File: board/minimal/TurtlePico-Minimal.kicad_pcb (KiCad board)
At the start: 2 copper layers, 121 parts, among them IC1 DRV8835DSSR, J1 Micro_SD, J10 LED, J11 LED, J12 Debug, J13 9DoF, J14 Temperature, J15 UltraSonic, J16 OLED, J2 USB_C_Receptacle_USB2.0_16P, J3 FR_ESC, J4 FL_ESC, J5 RMotor, J6 LMotor, J7 RR_ESC, J8 RL_ESC, J9 AudioJack3, Q1 DMP6050SSD, Q2 DMP6050SSD, Q3 2SC4213, Q4 2SC4213, SW1 SW_Bootsel, SW2 SW_RST, SW3 SW_{R}, SW4 SW_{L}, SW5 SW_DIP_x03, U1 W25Q128JVS, U10 PCM5102A, U2 AP63203WU, U3 RP2040, U4 STUSB4500QTR, U5 TLV73318PDBV, U6 PCA9306D, U7 ICM-20948, U8 BME280, U9 INA260, Y1 ABLS-12.000MHZ-B4-T

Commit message: set footprint
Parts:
- removed ? (x3): , 
- removed IC1: DRV8835DSSR, Package_SON:WSON-12-1EP_3x2mm_P0.5mm_EP1x2.65_ThermalVias
- removed Q4: 2SC4213, Package_TO_SOT_SMD:SOT-323_SC-70
- removed REF** (x4): MountingHole_3.2mm_M3_DIN965_Pad, MountingHole:MountingHole_3.2mm_M3_DIN965_Pad
- removed U10: PCM5102A, Package_SO:TSSOP-20_4.4x6.5mm_P0.65mm
- added C40: 0.01µ, Capacitor_SMD:C_0201_0603Metric, F.Cu at (123.6, 109.4)
- added C41: 10µ, Capacitor_SMD:CP_Elec_4x5.4, F.Cu at (109.4, 100.1)
- added C42: 10µ, Capacitor_SMD:CP_Elec_4x5.4, F.Cu at (109.4, 105.9)
- added C43: 10µ, Capacitor_SMD:CP_Elec_4x5.4, F.Cu at (109.4, 111.8)
- added J17: I/O Pins, Connector_PinSocket_2.54mm:PinSocket_2x08_P2.54mm_Vertical, F.Cu at (87.9, 41.2)
- added L2: 4.7u, AOTA-B201610S:L_pol_2016, F.Cu at (126.2, 66.8)
- added R30: 1k, Resistor_SMD:R_0603_1608Metric, F.Cu at (85.0, 74.6)
- added TP1: BNO_{BOOT}, TestPoint:TestPoint_Loop_D2.50mm_Drill1.85mm, F.Cu at (147.4, 94.0)
- added TP2: SPI_{MOSI}, TestPoint:TestPoint_Loop_D2.50mm_Drill1.85mm, F.Cu at (80.3, 41.6)
- added TP3: SPI_{SCK}, TestPoint:TestPoint_Loop_D2.50mm_Drill1.85mm, F.Cu at (80.3, 47.0)
- added TP4: SPI_{MISO}, TestPoint:TestPoint_Loop_D2.50mm_Drill1.85mm, F.Cu at (80.3, 52.5)
- added TP5: I2C_{SDA}, TestPoint:TestPoint_Loop_D2.50mm_Drill1.85mm, F.Cu at (80.3, 57.9)
- added TP6: I2C_{SCL}, TestPoint:TestPoint_Loop_D2.50mm_Drill1.85mm, F.Cu at (80.3, 63.4)
- added Y2: ABS06-32.768KHZ-T, ABRACON_Crystal:ABS06, F.Cu at (145.1, 107.7)
- C1, C2, C4, C6: value 100n -> 4.7u
- C12, C20, C3: value 1u -> 100n
- C14: value 10u -> 100n; footprint Capacitor_SMD:C_1206_3216Metric -> Capacitor_SMD:C_0201_0603Metric
- C15: value 22u -> 100n; footprint Capacitor_SMD:C_0402_1005Metric -> Capacitor_SMD:C_0201_0603Metric
- C16: value 22u -> 10u; footprint Capacitor_SMD:C_0402_1005Metric -> Capacitor_SMD:C_1206_3216Metric
- C17: value 27p -> 100n
- C18: value 27p -> 15p
- C19: value 1u -> 15p
- C21, C22: value 0.1u -> 22u; footprint Capacitor_SMD:C_0201_0603Metric -> Capacitor_SMD:C_0402_1005Metric
- C32, C33: value 0.01µ -> 100n
- C34, C35: value 10µ -> 20p; footprint Capacitor_SMD:CP_Elec_4x5.4 -> Capacitor_SMD:C_0201_0603Metric
- C36: value 10µ -> 2.2µ; footprint Capacitor_SMD:CP_Elec_4x5.4 -> Capacitor_SMD:C_0201_0603Metric
- C38: value 2.2µ -> 0.01µ
- J10: value LED -> AudioJack3; footprint Connector_PinSocket_2.54mm:PinSocket_1x02_P2.54mm_Vertical -> STX-3000:STX3000
- J12: value Debug -> LED; footprint Connector_JST:JST_PH_B3B-PH-SM4-TB_1x03-1MP_P2.00mm_Vertical -> Connector_PinSocket_2.54mm:PinSocket_1x02_P2.54mm_Vertical
- J13: value 9DoF -> UltraSonic; footprint Connector_JST:JST_XH_S4B-XH-A_1x04_P2.50mm_Horizontal -> Connector_PinSocket_2.54mm:PinSocket_1x04_P2.54mm_Vertical; moved to F.Cu
- J14: value Temperature -> Debug; footprint Connector_PinSocket_2.54mm:PinSocket_1x04_P2.54mm_Vertical -> Connector_JST:JST_PH_B3B-PH-SM4-TB_1x03-1MP_P2.00mm_Vertical
- J15: value UltraSonic -> Display; footprint Connector_PinSocket_2.54mm:PinSocket_1x04_P2.54mm_Vertical -> Connector_PinHeader_2.54mm:PinHeader_1x08_P2.54mm_Horizontal
- J16: value OLED -> TouchDisplay; footprint Connector_JST:JST_XH_S7B-XH-A_1x07_P2.50mm_Horizontal -> Connector_PinSocket_2.54mm:PinSocket_1x14_P2.54mm_Vertical; moved to F.Cu
- J2: value USB_C_Receptacle_USB2.0_16P -> Jack-DC; footprint Connector_USB:USB_C_Receptacle_GCT_USB4085 -> Connector_BarrelJack:BarrelJack_Horizontal; moved to F.Cu
- J3: value FR_ESC -> USB_C_Receptacle_USB2.0_16P; footprint Connector_PinHeader_2.54mm:PinHeader_1x03_P2.54mm_Horizontal -> Connector_USB:USB_C_Receptacle_GCT_USB4085; moved to F.Cu
- J4: value FL_ESC -> RMotor; footprint Connector_PinHeader_2.54mm:PinHeader_1x03_P2.54mm_Horizontal -> Connector_PinSocket_2.54mm:PinSocket_1x02_P2.54mm_Vertical; moved to F.Cu
- J5: value RMotor -> LMotor
- J6: value LMotor -> FR_ESC; footprint Connector_PinSocket_2.54mm:PinSocket_1x02_P2.54mm_Vertical -> Connector_PinHeader_2.54mm:PinHeader_1x03_P2.54mm_Horizontal
- J7: value RR_ESC -> FL_ESC; moved to F.Cu
- J8: value RL_ESC -> RR_ESC; moved to F.Cu
- J9: value AudioJack3 -> RL_ESC; footprint STX-3000:STX3000 -> Connector_PinHeader_2.54mm:PinHeader_1x03_P2.54mm_Horizontal; moved to F.Cu
- JP1: value I2C_Addr -> Jumper_Power; footprint Jumper:SolderJumper-2_P1.3mm_Open_RoundedPad1.0x1.5mm -> Connector_PinHeader_2.54mm:PinHeader_1x03_P2.54mm_Vertical
- JP2: value I2C_Addr -> Sens_SEL
- JP3: value Sens_SEL -> I2C_Addr
- L1: value 4.7u -> 3.3u; footprint Capacitor_SMD:C_0603_1608Metric -> AOTA-B201610S:L_pol_2016
- Q2: value DMP6050SSD -> 2SC4213; footprint Package_SO:SOIC-8_3.9x4.9mm_P1.27mm -> Package_TO_SOT_SMD:SOT-323_SC-70
- R1: value 27 -> 33
- R11: value 100k -> 1k
- R14, R21, R22: value 1k -> 10k
- R18: value 200k -> 100k
- R19: value 10k -> 1k
- R20: value 100k -> 10k
- R24, R25: value 5k -> 1k
- R26, R28: value 1k -> 5k
- R3, R7: value 1k -> 27
- R4, R5: value 10k -> 33
- R6: value 10k -> 27
- R8: value 1k -> 4.7k
- R9: value 10k -> 4.7k
- RV1: value 10k -> 50k; footprint Potentiometer_SMD:Potentiometer_ACP_CA6-VSMD_Vertical -> Potentiometer_THT:Potentiometer_Bourns_3339P_Vertical_HandSoldering
- SW2: value SW_RST -> SW_Reset
- SW5: value SW_DIP_x03 -> SW_DIP_x04; footprint DS04254203BKSMT:DS04254203BKSMT -> Package_DIP:DIP-8_W7.62mm
- U1: value W25Q128JVS -> RP2350B-QFN80; footprint Package_SO:SOIC-8_5.23x5.23mm_P1.27mm -> Package_DFN_QFN:QFN-80-1EP_10x10mm_P0.4mm_EP3.4x3.4mm_ThermalVias
- U2: value AP63203WU -> W25Q128JVS; footprint Package_TO_SOT_SMD:TSOT-23-6 -> Package_SO:SOIC-8_5.3x5.3mm_P1.27mm
- U3: value RP2040 -> AP63203WU; footprint Package_DFN_QFN:QFN-56-1EP_7x7mm_P0.4mm_EP3.2x3.2mm -> Package_TO_SOT_SMD:TSOT-23-6
- U5: value TLV73318PDBV -> DRV8835DSSR; footprint Package_TO_SOT_SMD:SOT-23-5 -> Package_SON:WSON-12-1EP_3x2mm_P0.5mm_EP1x2.65_ThermalVias
- U6: value PCA9306D -> INA260; footprint Package_SON:X2SON-8_1.4x1mm_P0.35mm -> Package_SO:TSSOP-16_4.4x5mm_P0.65mm
- U7: value ICM-20948 -> BNO086; footprint Sensor_Motion:InvenSense_QFN-24_3x3mm_P0.4mm -> BNO086:BNO086
- U9: value INA260 -> PCM5102A; footprint Package_SO:TSSOP-16_4.4x5mm_P0.65mm -> Package_SO:TSSOP-20_4.4x6.5mm_P0.65mm
- Y1: value ABLS-12.000MHZ-B4-T -> ABM8-272-T3; footprint ABLS-12_000MHZ-B4-T:ABLS -> ABRACON_Crystal:ABM8272T3
- moved J9 180.8 mm to (75.3, 109.8), turned to 0 degrees
- moved J7 179.2 mm to (75.3, 90.5)
- moved J16 175.1 mm to (75.3, 41.2), turned to 0 degrees
- moved J5 153.6 mm to (93.3, 80.8)
- moved J6 146.8 mm to (75.3, 80.8)
- moved J8 144.1 mm to (75.3, 100.1), turned to 0 degrees
- moved J14 143.2 mm to (89.3, 66.5), turned to 0 degrees
- moved J3 142.3 mm to (112.4, 53.1)
- moved J15 139.5 mm to (92.5, 41.2), turned to 0 degrees
- moved U4 133.0 mm to (129.8, 42.0)
- moved J13 132.1 mm to (97.8, 63.6)
- moved J4 132.0 mm to (88.7, 80.8), turned to 0 degrees
- moved J2 131.2 mm to (124.1, 44.2), turned to 0 degrees
- moved Y1 124.9 mm to (108.9, 82.8)
- moved R24 118.2 mm to (126.9, 107.0), turned to 0 degrees
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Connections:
- C1 pad 1: +1V1 -> +3.3V
- C13 pad 1: Net-(U2-BST) -> +3.3V
- C13 pad 2: Net-(U2-SW) -> GND
- C14 pad 1: VCC -> +3.3V
- C16 pad 1: +3.3V -> VCC
- C17 pad 1: GND -> +3.3V
- C17 pad 2: XIN -> GND
- C18 pad 2: Net-(C18-Pad2) -> XIN
- C19 pad 1: +2V8 -> GND
- C19 pad 2: GND -> Net-(C19-Pad2)
- C20 pad 1: Net-(U4-VREG_1V2) -> Net-(U3-BST)
- C20 pad 2: GND -> Net-(U3-SW)
- C21 pad 1: VCC -> +3.3V
- C23 pad 1: +3.3V -> +2V8
- C24 pad 1: +1V8 -> Net-(U4-VREG_1V2)
- C25 pad 1: +1V8 -> VBUS_{USB}
- C25 pad 2: GND -> Net-(C25-Pad2)
- C26 pad 1: +1V8 -> +3.3V
- C27 pad 1: Net-(U7-REGOUT) -> VCC
- C28 pad 1: +1V8 -> +3.3V
- C29 pad 1: +1V8 -> +3.3V
- C30 pad 1: Net-(JP3-A) -> GND
- C30 pad 2: Net-(C30-Pad2) -> Net-(U7-CAP)
- C32 pad 1: Net-(C32-Pad1) -> +3.3V
- C33 pad 1: Net-(C32-Pad1) -> +3.3V
- C34 pad 1: +3.3V -> GND
- C34 pad 2: GND -> Net-(U7-XOUT32/CLKSEL1)
- C35 pad 1: +3.3V -> GND
- C35 pad 2: GND -> Net-(U7-XIN32)
- C36 pad 1: +3.3V -> Net-(U9-CAPP)
- C36 pad 2: GND -> Net-(U9-CAPM)
- C37 pad 1: Net-(U10-CAPP) -> Net-(U9-VNEG)
- C37 pad 2: Net-(U10-CAPM) -> GND
- C38 pad 1: Net-(U10-VNEG) -> Net-(C38-Pad1)
- C39 pad 1: Net-(U10-LDOO) -> Net-(U9-LDOO)
- C4 pad 1: +3.3V -> Net-(U1-VREG_AVDD)
- C5 pad 1: +3.3V -> +1V1
- C6 pad 1: +3.3V -> +1V1
- D3 pad 2: LED_{L} -> LED_{R}
- D4 pad 2: LED_{R} -> LED_{L}
- J12 pad 1: SWD -> +3.3V
- J12 pad 2: GND -> Net-(J12-Pin_2)
- J13 pad 2: GND -> TRIG
- J13 pad 3: SDA -> Net-(J13-Pin_3)
- J13 pad 4: SCL -> GND
- J14 pad 1: +3.3V -> SWD
- J14 pad 2: SDA -> GND
- J14 pad 3: GND -> SW_{CLK}
- J15 pad 2: Tx/TRIG -> GND
- J15 pad 3: Net-(J15-Pin_3) -> SPI_{MOSI}
- J15 pad 4: GND -> SPI_{SCK}
- J16 pad 3: SPI_{MOSI} -> Display_{CS}
- J16 pad 4: SPI_{SCK} -> Display_{RST}
- J16 pad 5: OLED_{CS} -> Display_{DC}
- J16 pad 6: OLED_{DC} -> SPI_{MOSI}
- J16 pad 7: OLED_{RST} -> SPI_{SCK}
- J4 pad 1: GND -> Net-(J4-Pin_1)
- J4 pad 2: Net-(J3-Pin_2) -> Net-(J4-Pin_2)
- J5 pad 1: Net-(IC1-AOUT1) -> Net-(J5-Pin_1)
- J5 pad 2: Net-(IC1-AOUT2) -> Net-(J5-Pin_2)
- J6 pad 1: Net-(IC1-BOUT1) -> ESC_{FR}
- J6 pad 2: Net-(IC1-BOUT2) -> VCC
- J7 pad 1: ESC_{RR} -> GND
- J7 pad 2: Net-(J3-Pin_2) -> VCC
- J7 pad 3: GND -> ESC_{FL}
- J8 pad 1: GND -> ESC_{RR}
- J8 pad 2: Net-(J3-Pin_2) -> VCC
- J8 pad 3: ESC_{RL} -> GND
- JP1 pad 1: GND -> VBUS_{USB}
- JP1 pad 2: Net-(JP1-B) -> VBUS
- JP2 pad 1: GND -> VBUS
- JP2 pad 2: Net-(JP2-B) -> VCC
- JP3 pad 1: Net-(JP3-A) -> GND
- JP3 pad 2: VCC -> Net-(JP3-B)
- L1 pad 1: Net-(U2-SW) -> +1V1
- L1 pad 2: +3.3V -> Net-(U1-VREG_LX)
- Q1 pad 2: Net-(J3-Pin_2) -> PW_EN
- Q1 pad 4: Net-(J3-Pin_2) -> PW_EN
- Q1 pad 5: Net-(J3-Pin_2) -> VBUS_{USB}
- Q1 pad 6: Net-(J3-Pin_2) -> VBUS_{USB}
- Q1 pad 7: +3.3V -> Net-(Q1A-D1-Pad7)
- Q1 pad 8: +3.3V -> Net-(Q1A-D1-Pad7)
- Q2 pad 1: Net-(Q2A-S1) -> Net-(Q2-B)
- Q2 pad 2: PW_EN -> GND
- Q2 pad 3: Net-(Q2A-S1) -> Net-(J11-Pin_2)
- Q3 pad 3: Net-(J10-Pin_2) -> Net-(J12-Pin_2)
- R1 pad 1: D+ -> +3.3V
- R1 pad 2: Net-(U3-USB_DP) -> Net-(U1-VREG_AVDD)
- R10 pad 1: Net-(U4-DISCH) -> QSPI_{SS}
- R10 pad 2: VBUS -> Net-(R10-Pad2)
- R11 pad 1: Net-(J3-Pin_2) -> Net-(C19-Pad2)
- R11 pad 2: Net-(Q1A-S1) -> XOUT
- R12 pad 2: Net-(J3-Pin_2) -> Net-(R12-Pad2)
- R13 pad 1: +1V8 -> VBUS
- R13 pad 2: Net-(JP1-B) -> Net-(U4-VBUS_VS_DISCH)
- R14 pad 1: +1V8 -> Net-(U4-VBUS_EN_SNK)
- R14 pad 2: Net-(U6-SDA1) -> PW_EN
- R15 pad 1: +1V8 -> Net-(U4-POWER_OK2)
- R15 pad 2: Net-(U6-SCL1) -> Net-(D1-K)
- R16 pad 1: +3.3V -> Net-(U4-POWER_OK3)
- R16 pad 2: SCL -> Net-(D2-K)
- R17 pad 1: +3.3V -> Net-(U4-DISCH)
- R17 pad 2: SDA -> Net-(Q1A-D1-Pad7)
- R18 pad 1: +3.3V -> Net-(Q1A-S1)
- R18 pad 2: Net-(U6-EN) -> PW_EN
- R19 pad 1: +3.3V -> PW_EN
- R19 pad 2: Net-(JP2-B) -> Net-(C25-Pad2)
- R2 pad 1: D- -> D+0
- R2 pad 2: Net-(U3-USB_DM) -> Net-(U1-USB_DP)
- R20 pad 1: Net-(Q2A-S1) -> +3.3V
- R20 pad 2: PW_EN -> Net-(U7-BOOTN)
- R21 pad 1: PW_EN -> +3.3V
- R21 pad 2: Net-(C30-Pad2) -> Net-(U7-NRST)
- R22 pad 1: Net-(U10-OUTR) -> +3.3V
- R22 pad 2: Net-(C32-Pad1) -> Net-(JP3-B)
- R23 pad 1: Net-(U10-OUTL) -> Net-(U9-OUTL)
- R23 pad 2: Net-(C32-Pad1) -> Net-(C38-Pad1)
- R24 pad 1: Net-(Q3-B) -> Net-(U9-OUTR)
- R24 pad 2: LED_{R} -> Net-(C38-Pad1)
- R25 pad 1: Net-(Q4-B) -> GND
- R25 pad 2: LED_{L} -> Net-(D3-K)
- R26 pad 1: GND -> Net-(Q2-B)
- R26 pad 2: Net-(D3-K) -> LED_{R}
- R28 pad 1: Net-(J15-Pin_3) -> Net-(Q3-B)
- R28 pad 2: Rx/Echo -> LED_{L}
- R29 pad 2: Rx/Echo -> Echo
- R3 pad 1: QSPI_{SS} -> D-0
- R3 pad 2: Net-(R3-Pad2) -> Net-(U1-USB_DM)
- R4 pad 1: Run -> Net-(U1-GPIO8)
- R4 pad 2: Net-(R4-Pad2) -> SDA
- R5 pad 1: Net-(C18-Pad2) -> Net-(U1-GPIO9)
- R5 pad 2: XOUT -> SCL
- R6 pad 1: Net-(U4-VBUS_EN_SNK) -> D+1
- R6 pad 2: PW_EN -> Net-(U1-GPIO32)
- R7 pad 1: Net-(U4-POWER_OK2) -> D-1
- R7 pad 2: Net-(D1-K) -> Net-(U1-GPIO33)
- R8 pad 1: Net-(U4-POWER_OK3) -> SCL
- R8 pad 2: Net-(D2-K) -> +3.3V
- R9 pad 1: VBUS -> SDA
- R9 pad 2: Net-(U4-VBUS_VS_DISCH) -> +3.3V
- SW1 pad 1: Net-(R3-Pad2) -> Net-(R10-Pad2)
- SW2 pad 1: Net-(R4-Pad2) -> Net-(R12-Pad2)
- SW2 pad 2: GND -> +2V8
- SW5 pad 4: SW_{DIP}3 -> +3.3V
- SW5 pad 5: SW_{DIP}2 -> SW_{DIP}4
- SW5 pad 6: SW_{DIP}1 -> SW_{DIP}3
- U1 pad 1: QSPI_{SS} -> LED_{L}
- U1 pad 2: QSPI_{SD1} -> Display_{RST}
- U1 pad 3: QSPI_{SD2} -> Display_{DC}
- U1 pad 4: GND -> Display_{CS}
- U1 pad 5: QSPI_{SD0} -> +3.3V
- U1 pad 6: QSPI_{CLK} -> Net-(U1-GPIO8)
- U1 pad 7: QSPI_{SD3} -> Net-(U1-GPIO9)
- U1 pad 8: +3.3V -> SPI_{SCK}
- U2 pad 1: +3.3V -> QSPI_{SS}
- U2 pad 2: VCC -> QSPI_{SD1}
- U2 pad 3: VCC -> QSPI_{SD2}
- U2 pad 5: Net-(U2-SW) -> QSPI_{SD0}
- U2 pad 6: Net-(U2-BST) -> QSPI_{CLK}
- U3 pad 2: Rx/Echo -> VCC
- U3 pad 3: Tx/TRIG -> VCC
- U3 pad 4: ESC_{FL} -> GND
- U3 pad 5: SW_{L} -> Net-(U3-SW)
- U3 pad 6: LED_{L} -> Net-(U3-BST)
- U5 pad 1: +3.3V -> VCC
- U5 pad 2: GND -> Net-(J4-Pin_1)
- U5 pad 3: +3.3V -> Net-(J4-Pin_2)
- U5 pad 4: unconnected-(U5-NC-Pad4) -> Net-(J5-Pin_1)
- U5 pad 5: +1V8 -> Net-(J5-Pin_2)
- U6 pad 1: GND -> VBUS
- U6 pad 2: +1V8 -> VBUS
- U6 pad 3: Net-(U6-SCL1) -> VBUS
- U6 pad 4: Net-(U6-SDA1) -> GND
- U6 pad 5: SCL -> GND
- U6 pad 6: SDA -> GND
- U6 pad 7: Net-(U6-EN) -> unconnected-(U6-ALERT-Pad7)
- U6 pad 8: Net-(U6-EN) -> SDA
- U7 pad 10: Net-(U7-REGOUT) -> GND
- U7 pad 11: GND -> Net-(U7-NRST)
- U7 pad 13: +1V8 -> unconnected-(U7-RESV_NC_5-Pad13)
- U7 pad 17: unconnected-(U7-NC-Pad17) -> GND
- U7 pad 18: GND -> unconnected-(U7-H_CSN-Pad18)
- U7 pad 19: unconnected-(U7-RESV-Pad19) -> SCL
- U7 pad 2: unconnected-(U7-NC-Pad2) -> GND
- U7 pad 20: GND -> SDA
- U7 pad 22: +1V8 -> unconnected-(U7-RESV_NC_7-Pad22)
- U7 pad 23: Net-(U6-SCL1) -> unconnected-(U7-RESV_NC_8-Pad23)
- U7 pad 24: Net-(U6-SDA1) -> unconnected-(U7-RESV_NC_9-Pad24)
- U7 pad 3: unconnected-(U7-NC-Pad3) -> +3.3V
- U7 pad 4: unconnected-(U7-NC-Pad4) -> Net-(U7-BOOTN)
- U7 pad 5: unconnected-(U7-NC-Pad5) -> GND
- U7 pad 6: unconnected-(U7-NC-Pad6) -> GND
- U7 pad 8: +1V8 -> unconnected-(U7-RESV_NC_3-Pad8)
- U7 pad 9: Net-(JP1-B) -> Net-(U7-CAP)
- U8 pad 5: Net-(JP2-B) -> Net-(JP3-B)
- U9 pad 1: Net-(JP3-A) -> +3.3V
- U9 pad 10: +3.3V -> GND
- U9 pad 12: Net-(JP3-A) -> GND
- U9 pad 13: unconnected-(U9-NC-Pad13) -> I2S_{SCK}
- U9 pad 14: VCC -> I2S_{SD}
- U9 pad 15: VCC -> I2S_{WS}
- U9 pad 16: VCC -> GND
- U9 pad 2: Net-(JP3-A) -> Net-(U9-CAPP)
- U9 pad 3: Net-(JP3-A) -> GND
- U9 pad 4: GND -> Net-(U9-CAPM)
- U9 pad 5: GND -> Net-(U9-VNEG)
- U9 pad 6: GND -> Net-(U9-OUTL)
- U9 pad 7: unconnected-(U9-ALERT-Pad7) -> Net-(U9-OUTR)
- U9 pad 8: SDA -> +3.3V
- U9 pad 9: SCL -> GND
- Y1 pad 1: Net-(C18-Pad2) -> XIN
- Y1 pad 2: XIN -> GND

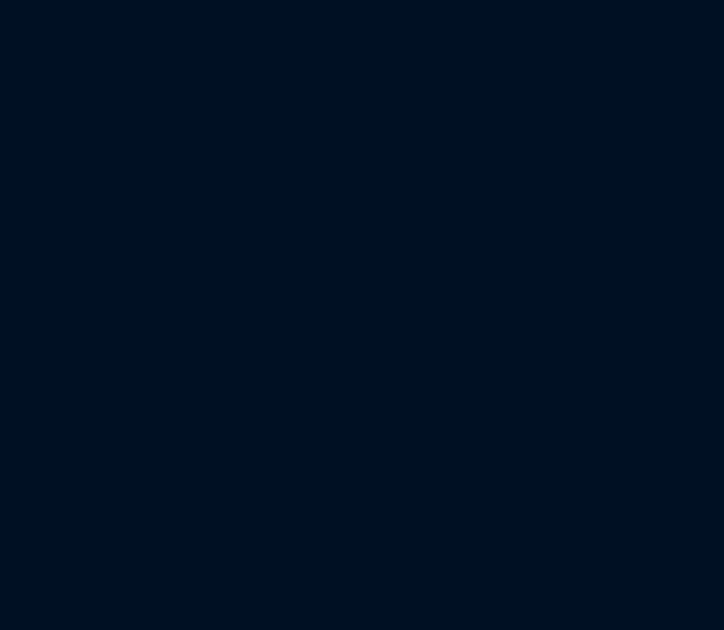
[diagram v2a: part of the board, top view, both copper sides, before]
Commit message: add testpoint for gnd and pic of schematics
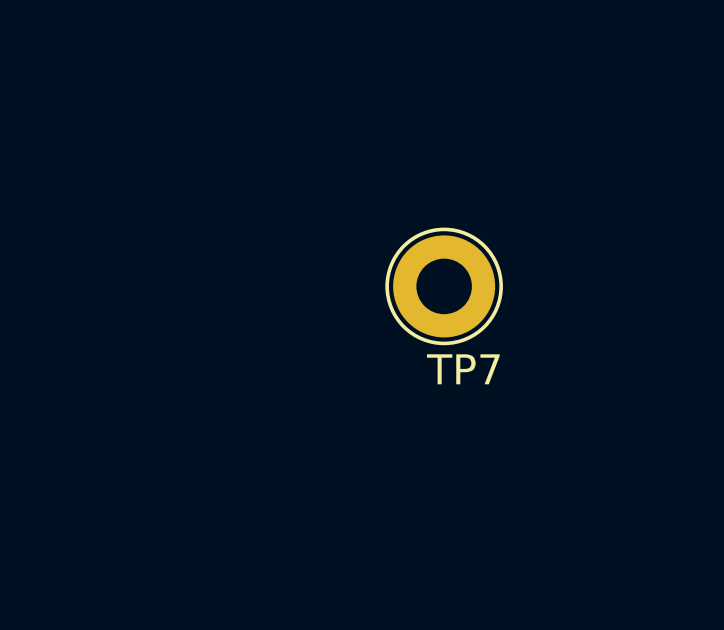
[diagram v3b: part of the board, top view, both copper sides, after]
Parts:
- added TP7: GND, TestPoint:TestPoint_Loop_D2.50mm_Drill1.85mm, F.Cu at (170.3, 57.9)
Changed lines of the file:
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@@
+		)
+	)
+	(footprint "TestPoint:TestPoint_Loop_D2.50mm_Drill1.85mm"
+		(layer "F.Cu")
+		(at 170.325 57.935)
+		(descr "wire loop as test point, loop diameter 2.5mm, hole diameter 1.85mm")
+		(tags "test point wire loop bead")
+		(property "Reference" "TP7"
+			(at 0.7 2.8 0)
+			(layer "F.SilkS")
+			(effects
+				(font
+					(size 1 1)
+					(thickness 0.15)
+				)
+			)
+		)
+		(property "Value" "GND"
+			(at 0 -2.8 0)
+			(layer "F.Fab")
+			(effects
+				(font
+					(size 1 1)
+					(thickness 0.15)
+				)
+			)
+		)
+		(property "Datasheet" ""
+			(at 0 0 0)
+			(unlocked yes)
+			(layer "F.Fab")
+			(hide yes)
+			(effects
+				(font
+					(size 1.27 1.27)
+					(thickness 0.15)
+				)
+			)
+		)
+		(property "Description" "test point"
+			(at 0 0 0)
+			(unlocked yes)
+			(layer "F.Fab")
+			(hide yes)
+			(effects
+				(font
+					(size 1.27 1.27)
+					(thickness 0.15)
+				)
+			)
+		)
+		(property ki_fp_filters "Pin* Test*")
+		(sheetname "/Connector/")
+		(sheetfile "Connector.kicad_sch")
+		(attr through_hole)
+		(duplicate_pad_numbers_are_jumpers no)
+		(fp_circle
+			(center 0 0)
+			(end 1.9 0)
+			(stroke
+				(width 0.12)
+				(type solid)
+			)
+			(fill no)
+			(layer "F.SilkS")
+		)
+		(fp_circle
+			(center 0 0)
+			(end 2.2 0)
+			(stroke
+				(width 0.05)
+				(type solid)
+			)
+			(fill no)
+			(layer "F.CrtYd")
+		)
+		(fp_line
+			(start -1.3 -0.2)
+			(end -1.3 0.2)
+			(stroke
+				(width 0.12)
+				(type solid)
+			)
+			(layer "F.Fab")
+		)
+		(fp_line
+			(start -1.3 0.2)
+			(end 1.3 0.2)
+			(stroke
+				(width 0.12)
+				(type solid)
+			)
+			(layer "F.Fab")
+		)
+		(fp_line
+			(start 1.3 -0.2)
+			(end -1.3 -0.2)
+			(stroke
+				(width 0.12)
+				(type solid)
+			)
+			(layer "F.Fab")
+		)
+		(fp_line
+			(start 1.3 0.2)
+			(end 1.3 -0.2)
+			(stroke
+				(width 0.12)
+				(type solid)
+			)
+			(layer "F.Fab")
+		)
+		(fp_text user "${REFERENCE}"
+			(at 0.7 2.8 0)
+			(layer "F.Fab")
+			(effects
+				(font
+					(size 1 1)
+					(thickness 0.15)
+				)
+			)
+		)
+		(pad "1" thru_hole circle
+			(at 0 0)
+			(size 3.4 3.4)
+			(drill 1.85)
+			(layers "*.Cu" "*.Mask")
+			(remove_unused_layers no)
+			(net 2 "GND")
+			(pinfunction "1")
+			(pintype "passive")
+			(tenting
+				(front none)
+				(back none)
+			)
+		)
+		(embedded_fonts no)
+		(model "${KICAD9_3DMODEL_DIR}/TestPoint.3dshapes/TestPoint_Loop_D2.50mm_Drill1.85mm.step"
+			(offset
+				(xyz 0 0 0)
+			)
+			(scale
+				(xyz 1 1 1)
+			)
+			(rotate
+				(xyz 0 0 0)
+			)
 		)
 	)
